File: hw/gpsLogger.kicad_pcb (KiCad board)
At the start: 2 copper layers, 41 x 72.8 mm, 46 parts, among them IC1 MSP430F55xx, P1 USB_OTG, Q2 FG6943010R, SW1 SW_PUSH, U1 MAX_M8Q, U2 MCP73812, U3 uSD, U6 TPS78230, X1 CRYSTAL_SMD

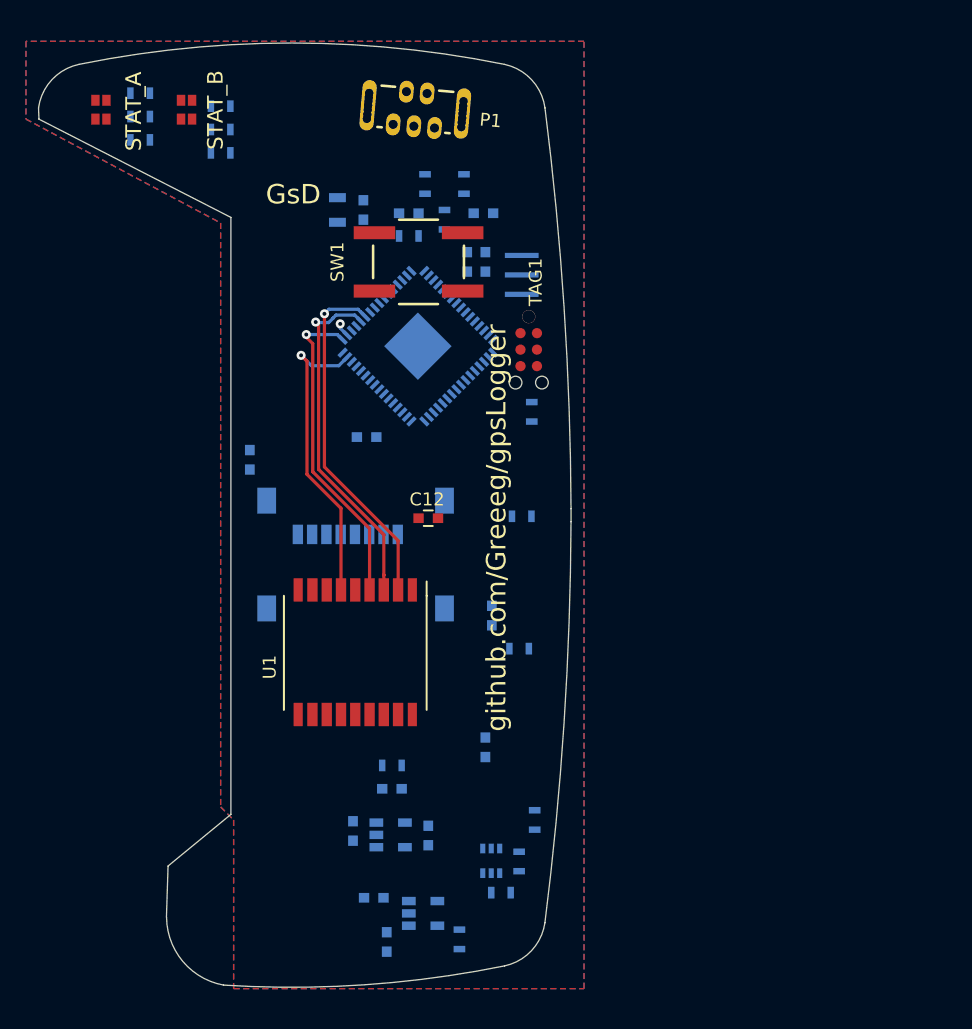
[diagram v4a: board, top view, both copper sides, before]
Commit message: Added mic2091 power switch. Began routing PCB
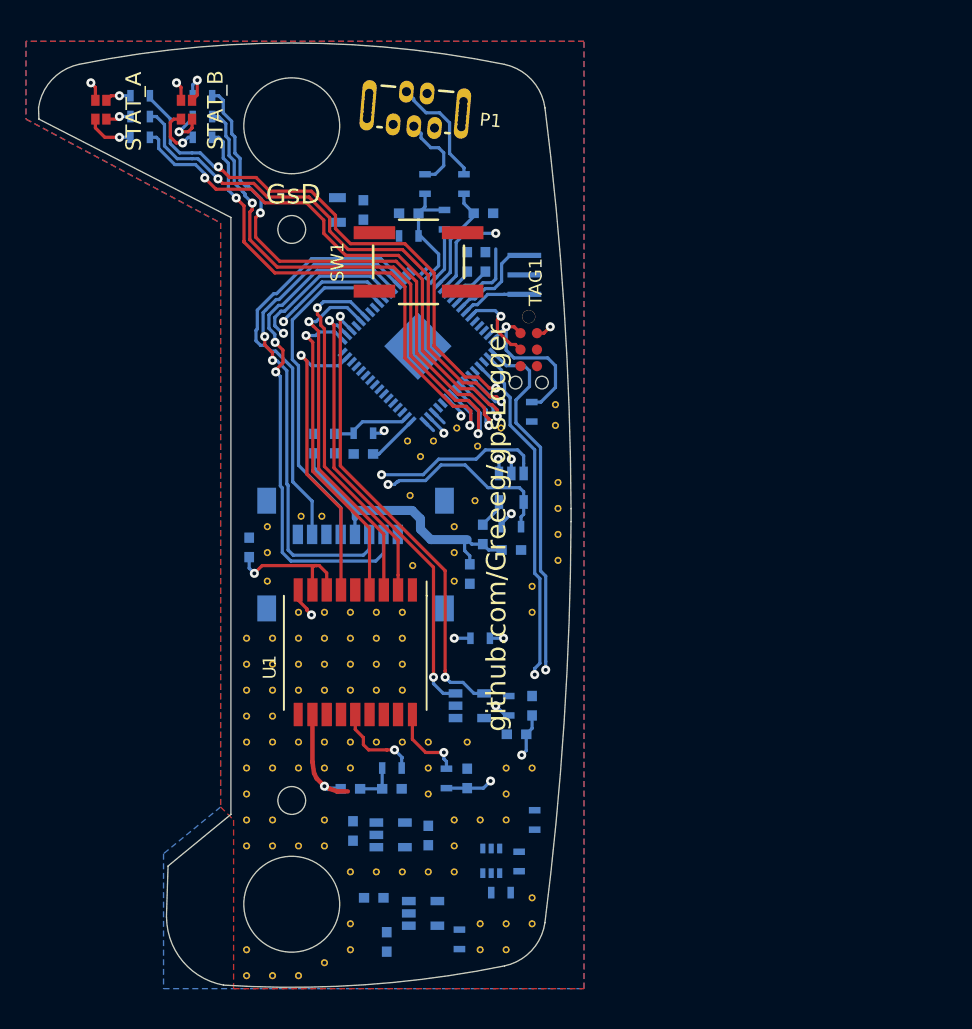
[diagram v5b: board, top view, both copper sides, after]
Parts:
- added C10: 100n, Capacitors_SMD:C_0603, B.Cu at (160.0, 116.2)
- added C11: 100n, Capacitors_SMD:C_0603, B.Cu at (144.8, 96.0)
- added C18: 100n, Capacitors_SMD:C_0603, B.Cu at (158.4, 104.2)
- added L1: 27nH, Capacitors_SMD:C_0603, B.Cu at (146.0, 122.6)
- added L2: 100nH, Capacitors_SMD:C_0603, B.Cu at (158.8, 118.4)
- added L3: 100nH, Capacitors_SMD:C_0603, B.Cu at (156.2, 103.0)
- added R10: 1k, Resistors_SMD:R_0603, B.Cu at (147.0, 95.2)
- added R11: 10k, Resistors_SMD:R_0603, B.Cu at (158.4, 102.4)
- added R9: 10k, Resistors_SMD:R_0603, B.Cu at (158.2, 116.2)
- added REF**: SolderWirePad_single_0-8mmDrill, Wire_Pads:SolderWirePad_single_0-8mmDrill, F.Cu at (150.6, 100.0)
- added REF**: SolderWirePad_single_0-8mmDrill, Wire_Pads:SolderWirePad_single_0-8mmDrill, F.Cu at (138.0, 135.0)
- added REF**: SolderWirePad_single_0-8mmDrill, Wire_Pads:SolderWirePad_single_0-8mmDrill, F.Cu at (150.8, 105.4)
- added REF**: SolderWirePad_single_0-8mmDrill, Wire_Pads:SolderWirePad_single_0-8mmDrill, F.Cu at (142.2, 101.6)
- added REF**: SolderWirePad_single_0-8mmDrill, Wire_Pads:SolderWirePad_single_0-8mmDrill, F.Cu at (143.8, 101.6)
- added REF**: SolderWirePad_single_0-8mmDrill, Wire_Pads:SolderWirePad_single_0-8mmDrill, F.Cu at (138.0, 137.0)
- added REF**: SolderWirePad_single_0-8mmDrill, Wire_Pads:SolderWirePad_single_0-8mmDrill, F.Cu at (140.0, 137.0)
- added REF**: SolderWirePad_single_0-8mmDrill, Wire_Pads:SolderWirePad_single_0-8mmDrill, F.Cu at (142.0, 137.0)
- added REF**: SolderWirePad_single_0-8mmDrill, Wire_Pads:SolderWirePad_single_0-8mmDrill, F.Cu at (146.0, 135.0)
- added REF**: SolderWirePad_single_0-8mmDrill, Wire_Pads:SolderWirePad_single_0-8mmDrill, F.Cu at (146.0, 133.0)
- added REF**: SolderWirePad_single_0-8mmDrill, Wire_Pads:SolderWirePad_single_0-8mmDrill, F.Cu at (160.0, 131.0)
- added REF**: SolderWirePad_single_0-8mmDrill, Wire_Pads:SolderWirePad_single_0-8mmDrill, F.Cu at (160.0, 133.0)
- added REF**: SolderWirePad_single_0-8mmDrill, Wire_Pads:SolderWirePad_single_0-8mmDrill, F.Cu at (156.0, 135.0)
- added REF**: SolderWirePad_single_0-8mmDrill, Wire_Pads:SolderWirePad_single_0-8mmDrill, F.Cu at (158.0, 135.0)
- added REF**: SolderWirePad_single_0-8mmDrill, Wire_Pads:SolderWirePad_single_0-8mmDrill, F.Cu at (155.6, 100.4)
- added REF**: SolderWirePad_single_0-8mmDrill, Wire_Pads:SolderWirePad_single_0-8mmDrill, F.Cu at (158.0, 133.0)
- added REF**: SolderWirePad_single_0-8mmDrill, Wire_Pads:SolderWirePad_single_0-8mmDrill, F.Cu at (156.0, 133.0)
- added REF**: SolderWirePad_single_0-8mmDrill, Wire_Pads:SolderWirePad_single_0-8mmDrill, F.Cu at (155.0, 119.0)
- added REF**: SolderWirePad_single_0-8mmDrill, Wire_Pads:SolderWirePad_single_0-8mmDrill, F.Cu at (160.0, 121.0)
- added REF**: SolderWirePad_single_0-8mmDrill, Wire_Pads:SolderWirePad_single_0-8mmDrill, F.Cu at (158.0, 121.0)
- added REF**: SolderWirePad_single_0-8mmDrill, Wire_Pads:SolderWirePad_single_0-8mmDrill, F.Cu at (158.0, 123.0)
- added REF**: SolderWirePad_single_0-8mmDrill, Wire_Pads:SolderWirePad_single_0-8mmDrill, F.Cu at (158.0, 125.0)
- added REF**: SolderWirePad_single_0-8mmDrill, Wire_Pads:SolderWirePad_single_0-8mmDrill, F.Cu at (152.0, 123.0)
- added REF**: SolderWirePad_single_0-8mmDrill, Wire_Pads:SolderWirePad_single_0-8mmDrill, F.Cu at (152.0, 121.0)
- added REF**: SolderWirePad_single_0-8mmDrill, Wire_Pads:SolderWirePad_single_0-8mmDrill, F.Cu at (152.0, 119.0)
- added REF**: SolderWirePad_single_0-8mmDrill, Wire_Pads:SolderWirePad_single_0-8mmDrill, F.Cu at (162.0, 99.0)
- added REF**: SolderWirePad_single_0-8mmDrill, Wire_Pads:SolderWirePad_single_0-8mmDrill, F.Cu at (156.0, 125.0)
- added REF**: SolderWirePad_single_0-8mmDrill, Wire_Pads:SolderWirePad_single_0-8mmDrill, F.Cu at (154.0, 125.0)
- added REF**: SolderWirePad_single_0-8mmDrill, Wire_Pads:SolderWirePad_single_0-8mmDrill, F.Cu at (154.0, 127.0)
- added REF**: SolderWirePad_single_0-8mmDrill, Wire_Pads:SolderWirePad_single_0-8mmDrill, F.Cu at (154.0, 129.0)
- added REF**: SolderWirePad_single_0-8mmDrill, Wire_Pads:SolderWirePad_single_0-8mmDrill, F.Cu at (152.0, 129.0)
- added REF**: SolderWirePad_single_0-8mmDrill, Wire_Pads:SolderWirePad_single_0-8mmDrill, F.Cu at (150.0, 129.0)
- added REF**: SolderWirePad_single_0-8mmDrill, Wire_Pads:SolderWirePad_single_0-8mmDrill, F.Cu at (148.0, 129.0)
- added REF**: SolderWirePad_single_0-8mmDrill, Wire_Pads:SolderWirePad_single_0-8mmDrill, F.Cu at (146.0, 129.0)
- added REF**: SolderWirePad_single_0-8mmDrill, Wire_Pads:SolderWirePad_single_0-8mmDrill, F.Cu at (138.0, 123.0)
- added REF**: SolderWirePad_single_0-8mmDrill, Wire_Pads:SolderWirePad_single_0-8mmDrill, F.Cu at (138.0, 125.0)
- added REF**: SolderWirePad_single_0-8mmDrill, Wire_Pads:SolderWirePad_single_0-8mmDrill, F.Cu at (162.0, 101.0)
- added REF**: SolderWirePad_single_0-8mmDrill, Wire_Pads:SolderWirePad_single_0-8mmDrill, F.Cu at (140.0, 125.0)
- added REF**: SolderWirePad_single_0-8mmDrill, Wire_Pads:SolderWirePad_single_0-8mmDrill, F.Cu at (144.0, 125.0)
- added REF**: SolderWirePad_single_0-8mmDrill, Wire_Pads:SolderWirePad_single_0-8mmDrill, F.Cu at (138.0, 127.0)
- added REF**: SolderWirePad_single_0-8mmDrill, Wire_Pads:SolderWirePad_single_0-8mmDrill, F.Cu at (140.0, 127.0)
- added REF**: SolderWirePad_single_0-8mmDrill, Wire_Pads:SolderWirePad_single_0-8mmDrill, F.Cu at (144.0, 127.0)
- added REF**: SolderWirePad_single_0-8mmDrill, Wire_Pads:SolderWirePad_single_0-8mmDrill, F.Cu at (142.0, 127.0)
- added REF**: SolderWirePad_single_0-8mmDrill, Wire_Pads:SolderWirePad_single_0-8mmDrill, F.Cu at (138.0, 121.0)
- added REF**: SolderWirePad_single_0-8mmDrill, Wire_Pads:SolderWirePad_single_0-8mmDrill, F.Cu at (140.0, 121.0)
- added REF**: SolderWirePad_single_0-8mmDrill, Wire_Pads:SolderWirePad_single_0-8mmDrill, F.Cu at (144.0, 121.0)
- added REF**: SolderWirePad_single_0-8mmDrill, Wire_Pads:SolderWirePad_single_0-8mmDrill, F.Cu at (142.0, 121.0)
- added REF**: SolderWirePad_single_0-8mmDrill, Wire_Pads:SolderWirePad_single_0-8mmDrill, F.Cu at (162.0, 103.0)
- added REF**: SolderWirePad_single_0-8mmDrill, Wire_Pads:SolderWirePad_single_0-8mmDrill, F.Cu at (146.0, 121.0)
- added REF**: SolderWirePad_single_0-8mmDrill, Wire_Pads:SolderWirePad_single_0-8mmDrill, F.Cu at (138.0, 111.0)
- added REF**: SolderWirePad_single_0-8mmDrill, Wire_Pads:SolderWirePad_single_0-8mmDrill, F.Cu at (138.0, 113.0)
- added REF**: SolderWirePad_single_0-8mmDrill, Wire_Pads:SolderWirePad_single_0-8mmDrill, F.Cu at (138.0, 117.0)
- added REF**: SolderWirePad_single_0-8mmDrill, Wire_Pads:SolderWirePad_single_0-8mmDrill, F.Cu at (138.0, 115.0)
- added REF**: SolderWirePad_single_0-8mmDrill, Wire_Pads:SolderWirePad_single_0-8mmDrill, F.Cu at (138.0, 119.0)
- added REF**: SolderWirePad_single_0-8mmDrill, Wire_Pads:SolderWirePad_single_0-8mmDrill, F.Cu at (140.0, 111.0)
- added REF**: SolderWirePad_single_0-8mmDrill, Wire_Pads:SolderWirePad_single_0-8mmDrill, F.Cu at (140.0, 113.0)
- added REF**: SolderWirePad_single_0-8mmDrill, Wire_Pads:SolderWirePad_single_0-8mmDrill, F.Cu at (140.0, 117.0)
- added REF**: SolderWirePad_single_0-8mmDrill, Wire_Pads:SolderWirePad_single_0-8mmDrill, F.Cu at (140.0, 115.0)
- added REF**: SolderWirePad_single_0-8mmDrill, Wire_Pads:SolderWirePad_single_0-8mmDrill, F.Cu at (162.0, 105.0)
- added REF**: SolderWirePad_single_0-8mmDrill, Wire_Pads:SolderWirePad_single_0-8mmDrill, F.Cu at (140.0, 119.0)
- added REF**: SolderWirePad_single_0-8mmDrill, Wire_Pads:SolderWirePad_single_0-8mmDrill, F.Cu at (150.0, 119.0)
- added REF**: SolderWirePad_single_0-8mmDrill, Wire_Pads:SolderWirePad_single_0-8mmDrill, F.Cu at (148.0, 119.0)
- added REF**: SolderWirePad_single_0-8mmDrill, Wire_Pads:SolderWirePad_single_0-8mmDrill, F.Cu at (144.0, 119.0)
- added REF**: SolderWirePad_single_0-8mmDrill, Wire_Pads:SolderWirePad_single_0-8mmDrill, F.Cu at (146.0, 119.0)
- added REF**: SolderWirePad_single_0-8mmDrill, Wire_Pads:SolderWirePad_single_0-8mmDrill, F.Cu at (142.0, 119.0)
- added REF**: SolderWirePad_single_0-8mmDrill, Wire_Pads:SolderWirePad_single_0-8mmDrill, F.Cu at (150.0, 115.0)
- added REF**: SolderWirePad_single_0-8mmDrill, Wire_Pads:SolderWirePad_single_0-8mmDrill, F.Cu at (148.0, 115.0)
- added REF**: SolderWirePad_single_0-8mmDrill, Wire_Pads:SolderWirePad_single_0-8mmDrill, F.Cu at (144.0, 115.0)
- added REF**: SolderWirePad_single_0-8mmDrill, Wire_Pads:SolderWirePad_single_0-8mmDrill, F.Cu at (146.0, 115.0)
- added REF**: SolderWirePad_single_0-8mmDrill, Wire_Pads:SolderWirePad_single_0-8mmDrill, F.Cu at (160.0, 107.0)
- added REF**: SolderWirePad_single_0-8mmDrill, Wire_Pads:SolderWirePad_single_0-8mmDrill, F.Cu at (142.0, 115.0)
- added REF**: SolderWirePad_single_0-8mmDrill, Wire_Pads:SolderWirePad_single_0-8mmDrill, F.Cu at (150.0, 113.0)
- added REF**: SolderWirePad_single_0-8mmDrill, Wire_Pads:SolderWirePad_single_0-8mmDrill, F.Cu at (148.0, 113.0)
- added REF**: SolderWirePad_single_0-8mmDrill, Wire_Pads:SolderWirePad_single_0-8mmDrill, F.Cu at (144.0, 113.0)
- added REF**: SolderWirePad_single_0-8mmDrill, Wire_Pads:SolderWirePad_single_0-8mmDrill, F.Cu at (146.0, 113.0)
- added REF**: SolderWirePad_single_0-8mmDrill, Wire_Pads:SolderWirePad_single_0-8mmDrill, F.Cu at (142.0, 113.0)
- added REF**: SolderWirePad_single_0-8mmDrill, Wire_Pads:SolderWirePad_single_0-8mmDrill, F.Cu at (150.0, 111.0)
- added REF**: SolderWirePad_single_0-8mmDrill, Wire_Pads:SolderWirePad_single_0-8mmDrill, F.Cu at (148.0, 111.0)
- added REF**: SolderWirePad_single_0-8mmDrill, Wire_Pads:SolderWirePad_single_0-8mmDrill, F.Cu at (144.0, 111.0)
- added REF**: SolderWirePad_single_0-8mmDrill, Wire_Pads:SolderWirePad_single_0-8mmDrill, F.Cu at (146.0, 111.0)
- added REF**: SolderWirePad_single_0-8mmDrill, Wire_Pads:SolderWirePad_single_0-8mmDrill, F.Cu at (160.0, 109.0)
- added REF**: SolderWirePad_single_0-8mmDrill, Wire_Pads:SolderWirePad_single_0-8mmDrill, F.Cu at (142.0, 111.0)
- added REF**: SolderWirePad_single_0-8mmDrill, Wire_Pads:SolderWirePad_single_0-8mmDrill, F.Cu at (150.0, 109.0)
- added REF**: SolderWirePad_single_0-8mmDrill, Wire_Pads:SolderWirePad_single_0-8mmDrill, F.Cu at (148.0, 109.0)
- added REF**: SolderWirePad_single_0-8mmDrill, Wire_Pads:SolderWirePad_single_0-8mmDrill, F.Cu at (146.0, 109.0)
- added REF**: SolderWirePad_single_0-8mmDrill, Wire_Pads:SolderWirePad_single_0-8mmDrill, F.Cu at (144.0, 109.0)
- added REF**: SolderWirePad_single_0-8mmDrill, Wire_Pads:SolderWirePad_single_0-8mmDrill, F.Cu at (142.0, 109.0)
- added REF**: SolderWirePad_single_0-8mmDrill, Wire_Pads:SolderWirePad_single_0-8mmDrill, F.Cu at (161.8, 94.6)
- added REF**: SolderWirePad_single_0-8mmDrill, Wire_Pads:SolderWirePad_single_0-8mmDrill, F.Cu at (161.8, 93.0)
- added REF**: SolderWirePad_single_0-8mmDrill, Wire_Pads:SolderWirePad_single_0-8mmDrill, F.Cu at (151.4, 97.0)
- added REF**: SolderWirePad_single_0-8mmDrill, Wire_Pads:SolderWirePad_single_0-8mmDrill, F.Cu at (150.4, 95.8)
- added REF**: SolderWirePad_single_0-8mmDrill, Wire_Pads:SolderWirePad_single_0-8mmDrill, F.Cu at (144.0, 136.0)
- added REF**: SolderWirePad_single_0-8mmDrill, Wire_Pads:SolderWirePad_single_0-8mmDrill, F.Cu at (155.8, 96.2)
- added REF**: SolderWirePad_single_0-8mmDrill, Wire_Pads:SolderWirePad_single_0-8mmDrill, F.Cu at (157.6, 94.8)
- added REF**: SolderWirePad_single_0-8mmDrill, Wire_Pads:SolderWirePad_single_0-8mmDrill, F.Cu at (152.4, 95.8)
- added REF**: SolderWirePad_single_0-8mmDrill, Wire_Pads:SolderWirePad_single_0-8mmDrill, F.Cu at (154.2, 94.8)
- added REF**: SolderWirePad_single_0-8mmDrill, Wire_Pads:SolderWirePad_single_0-8mmDrill, F.Cu at (154.0, 102.4)
- added REF**: SolderWirePad_single_0-8mmDrill, Wire_Pads:SolderWirePad_single_0-8mmDrill, F.Cu at (154.0, 104.4)
- added REF**: SolderWirePad_single_0-8mmDrill, Wire_Pads:SolderWirePad_single_0-8mmDrill, F.Cu at (154.0, 106.6)
- added REF**: SolderWirePad_single_0-8mmDrill, Wire_Pads:SolderWirePad_single_0-8mmDrill, F.Cu at (139.6, 104.4)
- added REF**: SolderWirePad_single_0-8mmDrill, Wire_Pads:SolderWirePad_single_0-8mmDrill, F.Cu at (139.6, 106.6)
- added REF**: SolderWirePad_single_0-8mmDrill, Wire_Pads:SolderWirePad_single_0-8mmDrill, F.Cu at (139.6, 102.4)
- added U4: MIC2091, TO_SOT_Packages_SMD:SOT-23-5, B.Cu at (155.2, 116.2)
- added U5: MIC2091, TO_SOT_Packages_SMD:SOT-23-5, B.Cu at (158.4, 99.4)
- C1, C7: value C -> 10n
- C12: value 100n -> 10n; moved to B.Cu
- C13: value 1u -> 1uF
- C16, C17, C4, C8: value C -> 1uF
- C2, C3: value C -> 22p
- FB1: value FILTER -> 1k FB
- R1, R2: value R -> 27R
- R3: value R -> 470k
- R4: value R -> 1k4
- moved R5 21.0 mm to (153.4, 121.8), turned to 270 degrees
- moved C12 14.0 mm to (138.2, 104.0), turned to 90 degrees
- moved C7 5.11 mm to (143.2, 96.0)
- moved C8 3.62 mm to (155.2, 106.0)
- moved R8 3.10 mm to (156.0, 111.0)
- moved C13 2.78 mm to (155.0, 121.8), turned to 90 degrees
- moved R21 1.84 mm to (134.6, 72.4)
- moved R20 1.72 mm to (134.6, 70.8)
- moved R19 1.61 mm to (134.6, 69.2)
- moved C4 1.32 mm to (147.0, 96.8)
- moved X1 0.20 mm to (159.4, 83.0)
- moved R16 0.20 mm to (129.8, 69.2)
- moved R6 0.20 mm to (149.2, 121.0)
- moved R18 0.20 mm to (129.8, 72.4)
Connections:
- net /GPS_FIX renamed Net-(IC1-Pad32)
- net /NEW_BUT renamed Net-(IC1-Pad19)
- net /SD_CLK renamed MMC_CLK
- net /SD_CS renamed MMC_CS
- net /SD_MISO renamed MMC_MISO
- net /SD_MOSI renamed MMC_MOSI
- net /SD_VCC renamed MMC_VCC
- IC1 pad 18: /PWR_BUT -> PWR_BUT
- IC1 pad 34: /GPS_PWR -> GPS_PWR
- IC1 pad 35: Net-(IC1-Pad35) -> GPS_PWR_FAULT
- IC1 pad 42: /SD_PWR -> MMC_PWR
- IC1 pad 43: Net-(IC1-Pad43) -> MMC_PWR_FAULT
- IC1 pad 52: /DM -> Net-(IC1-Pad52)
- SW1 pad 1: /PWR_BUT -> Net-(R10-Pad2)
- U2 pad 1: VBUS -> ~CHG
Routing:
- net GPS_VCC: track 0.00 -> 56.9 mm, vias 0 -> 4
- net /LED_B_R: track 0.00 -> 44.9 mm, vias 0 -> 2
- net MMC_PWR_FAULT: track 0.00 -> 44.3 mm, vias 0 -> 2
- net /LED_A_G: track 0.00 -> 44.3 mm, vias 0 -> 2
- net /LED_A_B: track 0.00 -> 44.2 mm, vias 0 -> 2
- net /LED_B_G: track 0.00 -> 43.5 mm, vias 0 -> 2
- net /LED_A_R: track 0.00 -> 43.4 mm, vias 0 -> 2
- net MMC_CS: track 0.00 -> 40.6 mm, vias 0 -> 2
- net MMC_PWR: track 0.00 -> 40.1 mm, vias 0 -> 2
- net /LED_B_B: track 0.00 -> 39.7 mm, vias 0 -> 2
- net MMC_MOSI: track 0.00 -> 39.6 mm, vias 0 -> 2
- net GPS_PWR_FAULT: track 0.00 -> 36.1 mm, vias 0 -> 2
- net GPS_PWR: track 0.00 -> 35.1 mm, vias 0 -> 2
- net MMC_MISO: track 0.00 -> 33.0 mm
- net /V_SENSE: track 0.00 -> 27.8 mm, vias 0 -> 1
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- added copper zone on In1.Cu, net +3V3
- added copper zone on In1.Cu, net GND
- added copper zone on In2.Cu, net GND
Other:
- outline, holes or cut-outs redrawn
- copper layers 2 -> 4

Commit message: Finished Initial routing
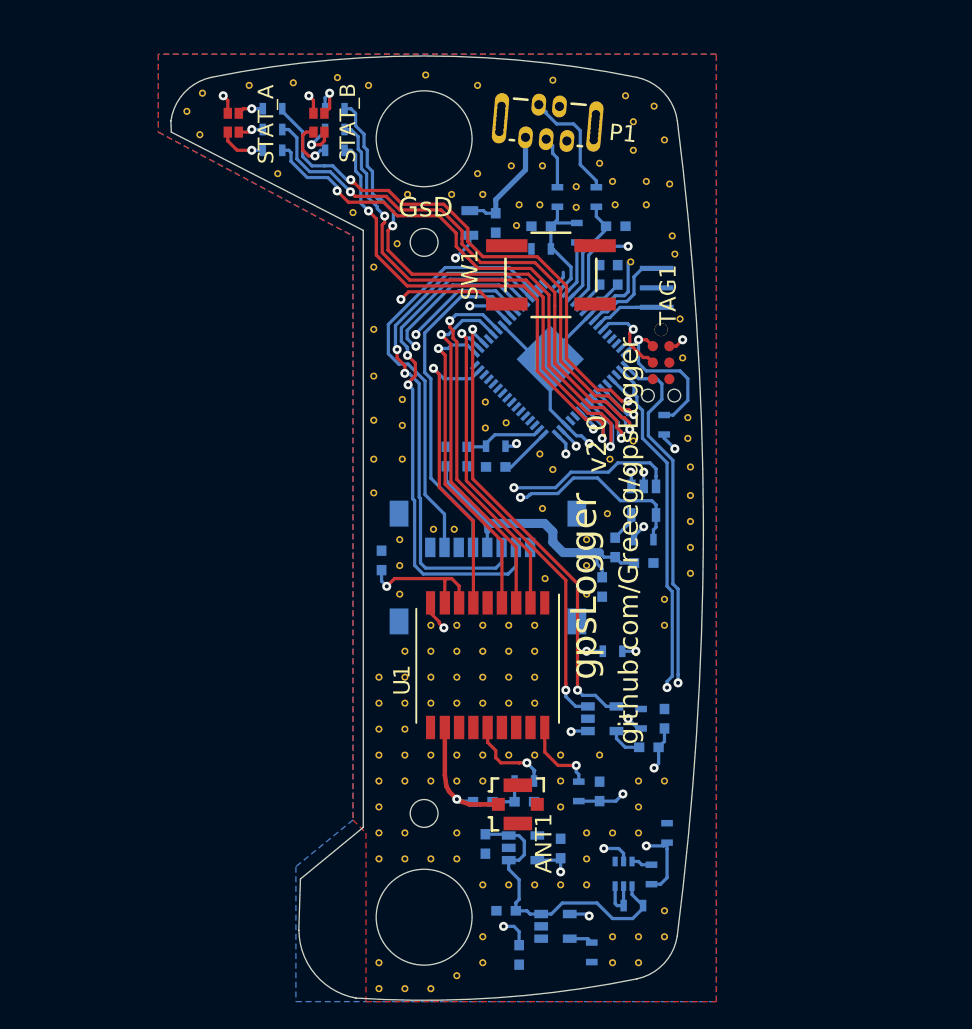
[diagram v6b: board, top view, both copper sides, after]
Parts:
- removed the REF** at (138.0, 111.0)
- removed the REF** at (152.4, 95.8)
- removed the REF** at (154.2, 94.8)
- added ANT1: ANT, footprints:MCRF, F.Cu at (158.9, 123.8)
- added REF**: SolderWirePad_single_0-8mmDrill, Wire_Pads:SolderWirePad_single_0-8mmDrill, F.Cu at (172.2, 97.8)
- added REF**: SolderWirePad_single_0-8mmDrill, Wire_Pads:SolderWirePad_single_0-8mmDrill, F.Cu at (159.0, 77.6)
- added REF**: SolderWirePad_single_0-8mmDrill, Wire_Pads:SolderWirePad_single_0-8mmDrill, F.Cu at (160.6, 77.6)
- added REF**: SolderWirePad_single_0-8mmDrill, Wire_Pads:SolderWirePad_single_0-8mmDrill, F.Cu at (163.4, 77.8)
- added REF**: SolderWirePad_single_0-8mmDrill, Wire_Pads:SolderWirePad_single_0-8mmDrill, F.Cu at (163.4, 76.2)
- added REF**: SolderWirePad_single_0-8mmDrill, Wire_Pads:SolderWirePad_single_0-8mmDrill, F.Cu at (160.8, 74.6)
- added REF**: SolderWirePad_single_0-8mmDrill, Wire_Pads:SolderWirePad_single_0-8mmDrill, F.Cu at (167.8, 71.2)
- added REF**: SolderWirePad_single_0-8mmDrill, Wire_Pads:SolderWirePad_single_0-8mmDrill, F.Cu at (167.8, 73.4)
- added REF**: SolderWirePad_single_0-8mmDrill, Wire_Pads:SolderWirePad_single_0-8mmDrill, F.Cu at (168.8, 75.8)
- added REF**: SolderWirePad_single_0-8mmDrill, Wire_Pads:SolderWirePad_single_0-8mmDrill, F.Cu at (168.8, 77.6)
- added REF**: SolderWirePad_single_0-8mmDrill, Wire_Pads:SolderWirePad_single_0-8mmDrill, F.Cu at (166.4, 77.6)
- added REF**: SolderWirePad_single_0-8mmDrill, Wire_Pads:SolderWirePad_single_0-8mmDrill, F.Cu at (171.6, 89.4)
- added REF**: SolderWirePad_single_0-8mmDrill, Wire_Pads:SolderWirePad_single_0-8mmDrill, F.Cu at (166.2, 75.8)
- added REF**: SolderWirePad_single_0-8mmDrill, Wire_Pads:SolderWirePad_single_0-8mmDrill, F.Cu at (165.2, 74.4)
- added REF**: SolderWirePad_single_0-8mmDrill, Wire_Pads:SolderWirePad_single_0-8mmDrill, F.Cu at (170.8, 80.0)
- added REF**: SolderWirePad_single_0-8mmDrill, Wire_Pads:SolderWirePad_single_0-8mmDrill, F.Cu at (170.6, 76.0)
- added REF**: SolderWirePad_single_0-8mmDrill, Wire_Pads:SolderWirePad_single_0-8mmDrill, F.Cu at (170.2, 72.6)
- added REF**: SolderWirePad_single_0-8mmDrill, Wire_Pads:SolderWirePad_single_0-8mmDrill, F.Cu at (169.4, 70.0)
- added REF**: SolderWirePad_single_0-8mmDrill, Wire_Pads:SolderWirePad_single_0-8mmDrill, F.Cu at (167.2, 69.2)
- added REF**: SolderWirePad_single_0-8mmDrill, Wire_Pads:SolderWirePad_single_0-8mmDrill, F.Cu at (140.4, 75.2)
- added REF**: SolderWirePad_single_0-8mmDrill, Wire_Pads:SolderWirePad_single_0-8mmDrill, F.Cu at (134.4, 72.2)
- added REF**: SolderWirePad_single_0-8mmDrill, Wire_Pads:SolderWirePad_single_0-8mmDrill, F.Cu at (133.4, 70.4)
- added REF**: SolderWirePad_single_0-8mmDrill, Wire_Pads:SolderWirePad_single_0-8mmDrill, F.Cu at (171.0, 81.4)
- added REF**: SolderWirePad_single_0-8mmDrill, Wire_Pads:SolderWirePad_single_0-8mmDrill, F.Cu at (134.6, 69.0)
- added REF**: SolderWirePad_single_0-8mmDrill, Wire_Pads:SolderWirePad_single_0-8mmDrill, F.Cu at (145.0, 67.8)
- added REF**: SolderWirePad_single_0-8mmDrill, Wire_Pads:SolderWirePad_single_0-8mmDrill, F.Cu at (141.6, 68.2)
- added REF**: SolderWirePad_single_0-8mmDrill, Wire_Pads:SolderWirePad_single_0-8mmDrill, F.Cu at (138.2, 68.4)
- added REF**: SolderWirePad_single_0-8mmDrill, Wire_Pads:SolderWirePad_single_0-8mmDrill, F.Cu at (147.4, 68.4)
- added REF**: SolderWirePad_single_0-8mmDrill, Wire_Pads:SolderWirePad_single_0-8mmDrill, F.Cu at (151.8, 67.6)
- added REF**: SolderWirePad_single_0-8mmDrill, Wire_Pads:SolderWirePad_single_0-8mmDrill, F.Cu at (155.8, 68.4)
- added REF**: SolderWirePad_single_0-8mmDrill, Wire_Pads:SolderWirePad_single_0-8mmDrill, F.Cu at (155.8, 75.2)
- added REF**: SolderWirePad_single_0-8mmDrill, Wire_Pads:SolderWirePad_single_0-8mmDrill, F.Cu at (153.8, 76.8)
- added REF**: SolderWirePad_single_0-8mmDrill, Wire_Pads:SolderWirePad_single_0-8mmDrill, F.Cu at (150.4, 76.8)
- added REF**: SolderWirePad_single_0-8mmDrill, Wire_Pads:SolderWirePad_single_0-8mmDrill, F.Cu at (171.4, 86.4)
- added REF**: SolderWirePad_single_0-8mmDrill, Wire_Pads:SolderWirePad_single_0-8mmDrill, F.Cu at (146.2, 78.2)
- added REF**: SolderWirePad_single_0-8mmDrill, Wire_Pads:SolderWirePad_single_0-8mmDrill, F.Cu at (149.6, 80.6)
- added REF**: SolderWirePad_single_0-8mmDrill, Wire_Pads:SolderWirePad_single_0-8mmDrill, F.Cu at (147.8, 82.4)
- added REF**: SolderWirePad_single_0-8mmDrill, Wire_Pads:SolderWirePad_single_0-8mmDrill, F.Cu at (147.8, 87.2)
- added REF**: SolderWirePad_single_0-8mmDrill, Wire_Pads:SolderWirePad_single_0-8mmDrill, F.Cu at (147.8, 90.8)
- added REF**: SolderWirePad_single_0-8mmDrill, Wire_Pads:SolderWirePad_single_0-8mmDrill, F.Cu at (147.8, 94.2)
- added REF**: SolderWirePad_single_0-8mmDrill, Wire_Pads:SolderWirePad_single_0-8mmDrill, F.Cu at (147.8, 97.2)
- added REF**: SolderWirePad_single_0-8mmDrill, Wire_Pads:SolderWirePad_single_0-8mmDrill, F.Cu at (147.8, 99.8)
- added REF**: SolderWirePad_single_0-8mmDrill, Wire_Pads:SolderWirePad_single_0-8mmDrill, F.Cu at (150.0, 97.2)
- added REF**: SolderWirePad_single_0-8mmDrill, Wire_Pads:SolderWirePad_single_0-8mmDrill, F.Cu at (150.0, 94.6)
- added REF**: SolderWirePad_single_0-8mmDrill, Wire_Pads:SolderWirePad_single_0-8mmDrill, F.Cu at (167.6, 82.0)
- added REF**: SolderWirePad_single_0-8mmDrill, Wire_Pads:SolderWirePad_single_0-8mmDrill, F.Cu at (150.0, 92.6)
- added REF**: SolderWirePad_single_0-8mmDrill, Wire_Pads:SolderWirePad_single_0-8mmDrill, F.Cu at (158.0, 94.4)
- added REF**: SolderWirePad_single_0-8mmDrill, Wire_Pads:SolderWirePad_single_0-8mmDrill, F.Cu at (156.4, 92.8)
- added REF**: SolderWirePad_single_0-8mmDrill, Wire_Pads:SolderWirePad_single_0-8mmDrill, F.Cu at (156.4, 94.8)
- added REF**: SolderWirePad_single_0-8mmDrill, Wire_Pads:SolderWirePad_single_0-8mmDrill, F.Cu at (161.6, 68.0)
- added REF**: SolderWirePad_single_0-8mmDrill, Wire_Pads:SolderWirePad_single_0-8mmDrill, F.Cu at (158.4, 74.6)
- added REF**: SolderWirePad_single_0-8mmDrill, Wire_Pads:SolderWirePad_single_0-8mmDrill, F.Cu at (156.2, 76.8)
- added REF**: SolderWirePad_single_0-8mmDrill, Wire_Pads:SolderWirePad_single_0-8mmDrill, F.Cu at (158.8, 79.2)
- moved C12 10.2 mm to (148.4, 105.0)
- moved C14 10.2 mm to (156.4, 126.8)
- moved C5 10.2 mm to (159.4, 123.6)
- moved C7 10.2 mm to (153.4, 97.0)
- moved C8 10.2 mm to (165.4, 107.0)
- moved L3 10.2 mm to (166.4, 104.0)
- moved R12 10.2 mm to (167.8, 131.6)
- moved R14 10.2 mm to (170.4, 126.0)
- moved R15 10.2 mm to (170.2, 94.5)
- moved R19 10.2 mm to (144.8, 70.2)
- moved R20 10.2 mm to (144.8, 71.8)
- moved R21 10.2 mm to (144.8, 73.4)
- moved R6 10.2 mm to (159.4, 122.0)
- moved R9 10.2 mm to (168.4, 117.2)
- moved REF** 10.2 mm to (167.8, 95.8)
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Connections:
- IC1 pad 65: (no net) -> GND
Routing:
- net VBUS: track 7.39 -> 97.2 mm, vias 1 -> 4
- net Net-(R10-Pad2): track 0.93 -> 29.2 mm, vias 1 -> 2
- net /V_SENSE: track 27.8 -> 51.4 mm, vias 1 -> 2
- net +BATT: track 0.00 -> 23.1 mm
- net GND: track 9.36 -> 29.7 mm, vias 1 -> 3
- net /SENSE_EN: track 26.3 -> 43.4 mm, vias 1 -> 2
- net +3V3: track 11.5 -> 25.3 mm, vias 8 -> 12
- net Net-(C1-Pad1): track 0.00 -> 8.88 mm
- net Net-(Q2-Pad5): track 0.00 -> 3.56 mm
- net Net-(L2-Pad1): track 0.00 -> 2.60 mm
- net /D+: track 6.07 -> 4.06 mm
- net Net-(R7-Pad2): track 0.00 -> 1.82 mm
- net Net-(Q2-Pad3): track 0.00 -> 1.60 mm
- net GPS_RF_IN: track 9.04 -> 10.4 mm
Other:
- board text added: "gpsLogger"
- board text added: "v2.0"
